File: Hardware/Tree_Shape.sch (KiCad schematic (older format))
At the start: 162 parts

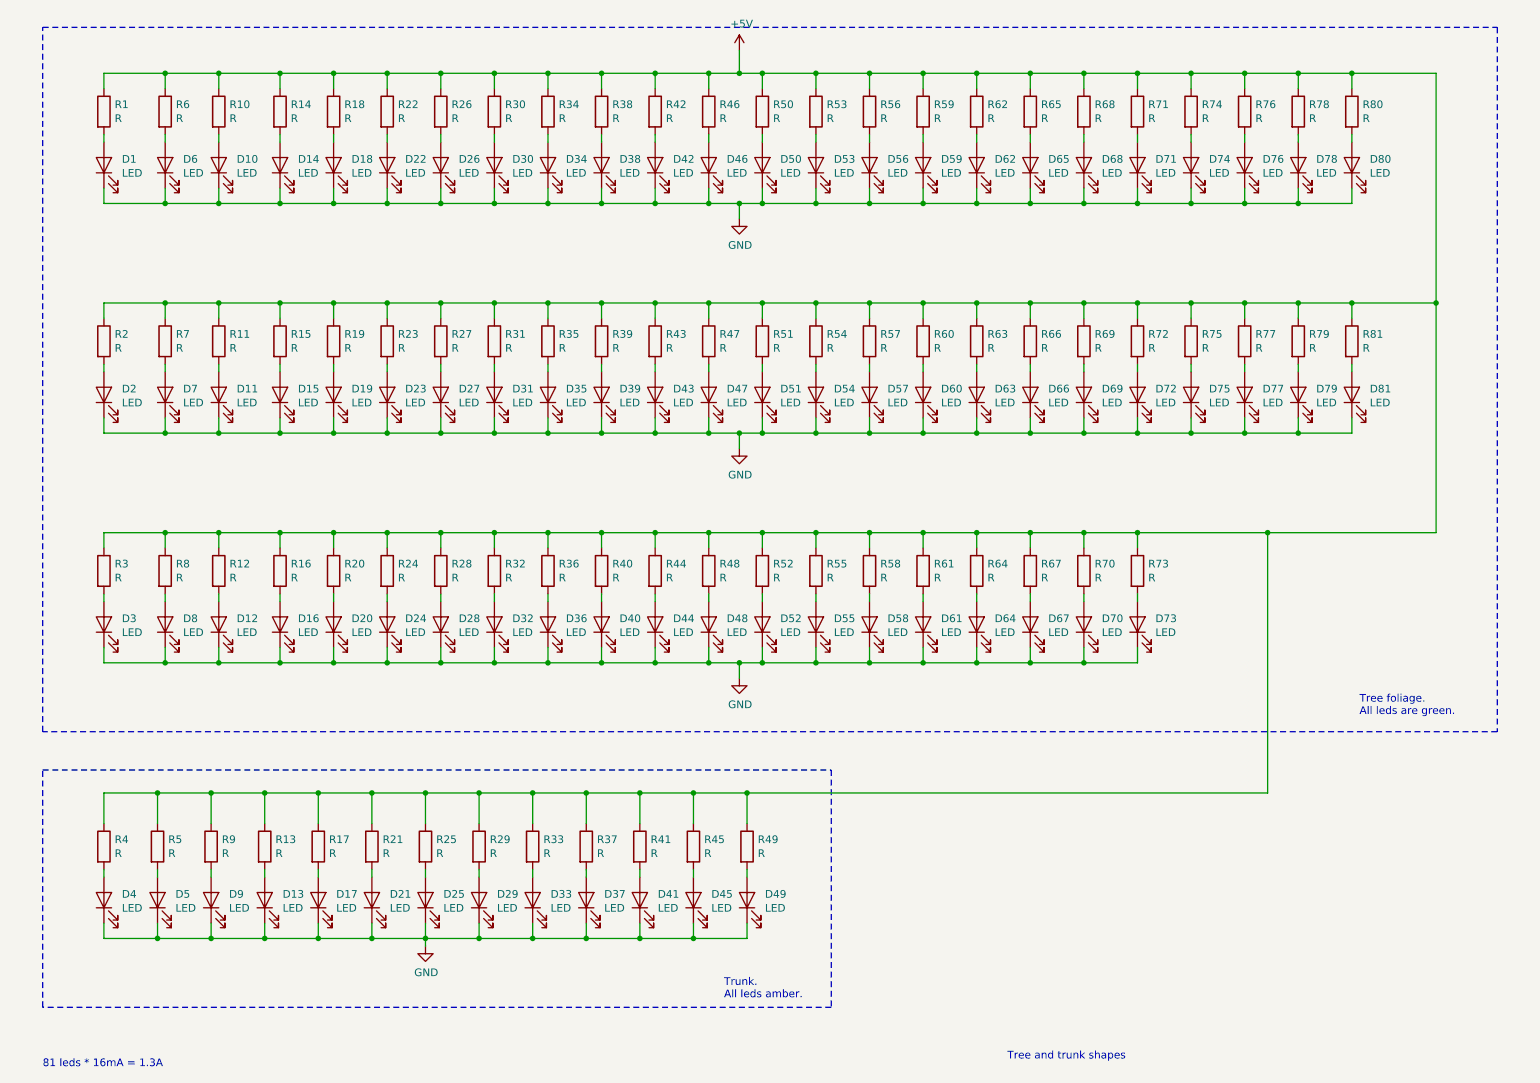
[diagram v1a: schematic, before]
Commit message: Set foliage and trunk leds color.
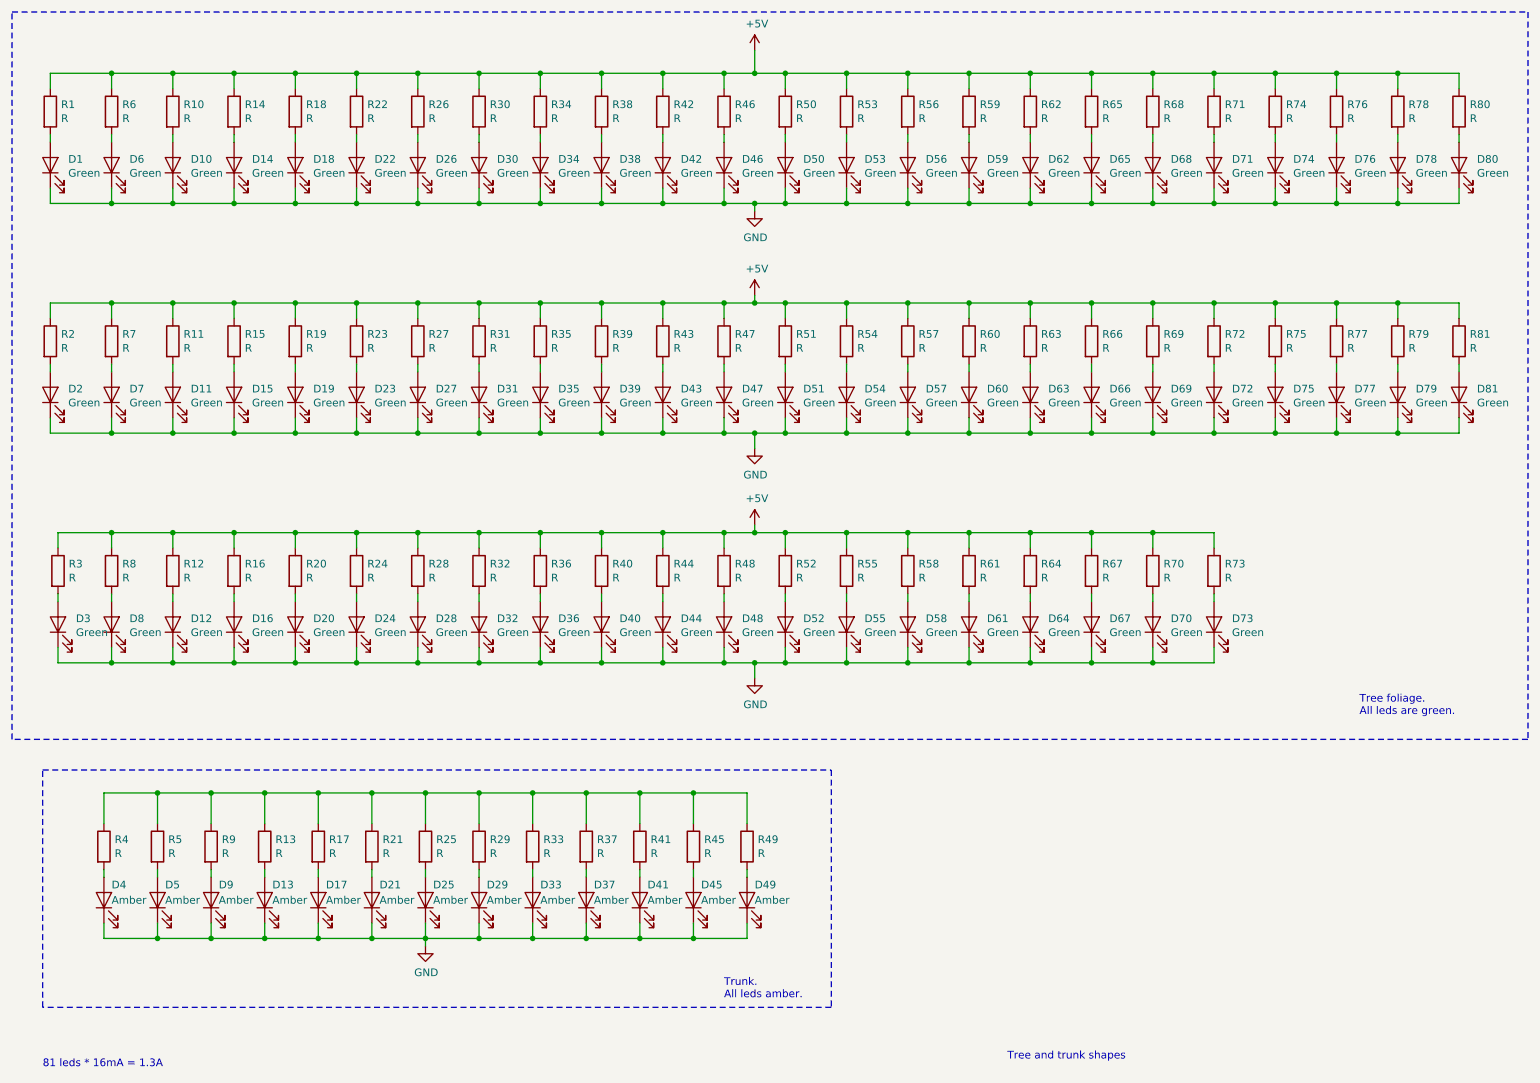
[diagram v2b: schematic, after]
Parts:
- D1, D10, D11, D12, D14, D15, D16, D18, D19, D2, D20, D22, D23, D24, D26, D27, D28, D3, D30, D31, D32, D34, D35, D36, D38, D39, D40, D42, D43, D44, D46, D47, D48, D50, D51, D52, D53, D54, D55, D56, D57, D58, D59, D6, D60, D61, D62, D63, D64, D65, D66, D67, D68, D69, D7, D70, D71, D72, D73, D74, D75, D76, D77, D78, D79, D8, D80, D81: value LED -> Green
- D13, D17, D21, D25, D29, D33, D37, D4, D41, D45, D49, D5, D9: value LED -> Amber
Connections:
- net +5V: no longer R13.1, R17.1, R21.1, R25.1, R29.1, R33.1, R37.1, R4.1, R41.1, R45.1, R49.1, R5.1, R9.1
- new net: R13.1, R17.1, R21.1, R25.1, R29.1, R33.1, R37.1, R4.1, R41.1, R45.1, R49.1, R5.1, R9.1
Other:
- moved on the sheet: D1, D10, D11, D12, D14, D15, D16, D18, D19, D2, D20, D22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

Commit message: Set foliage leds resistors value.
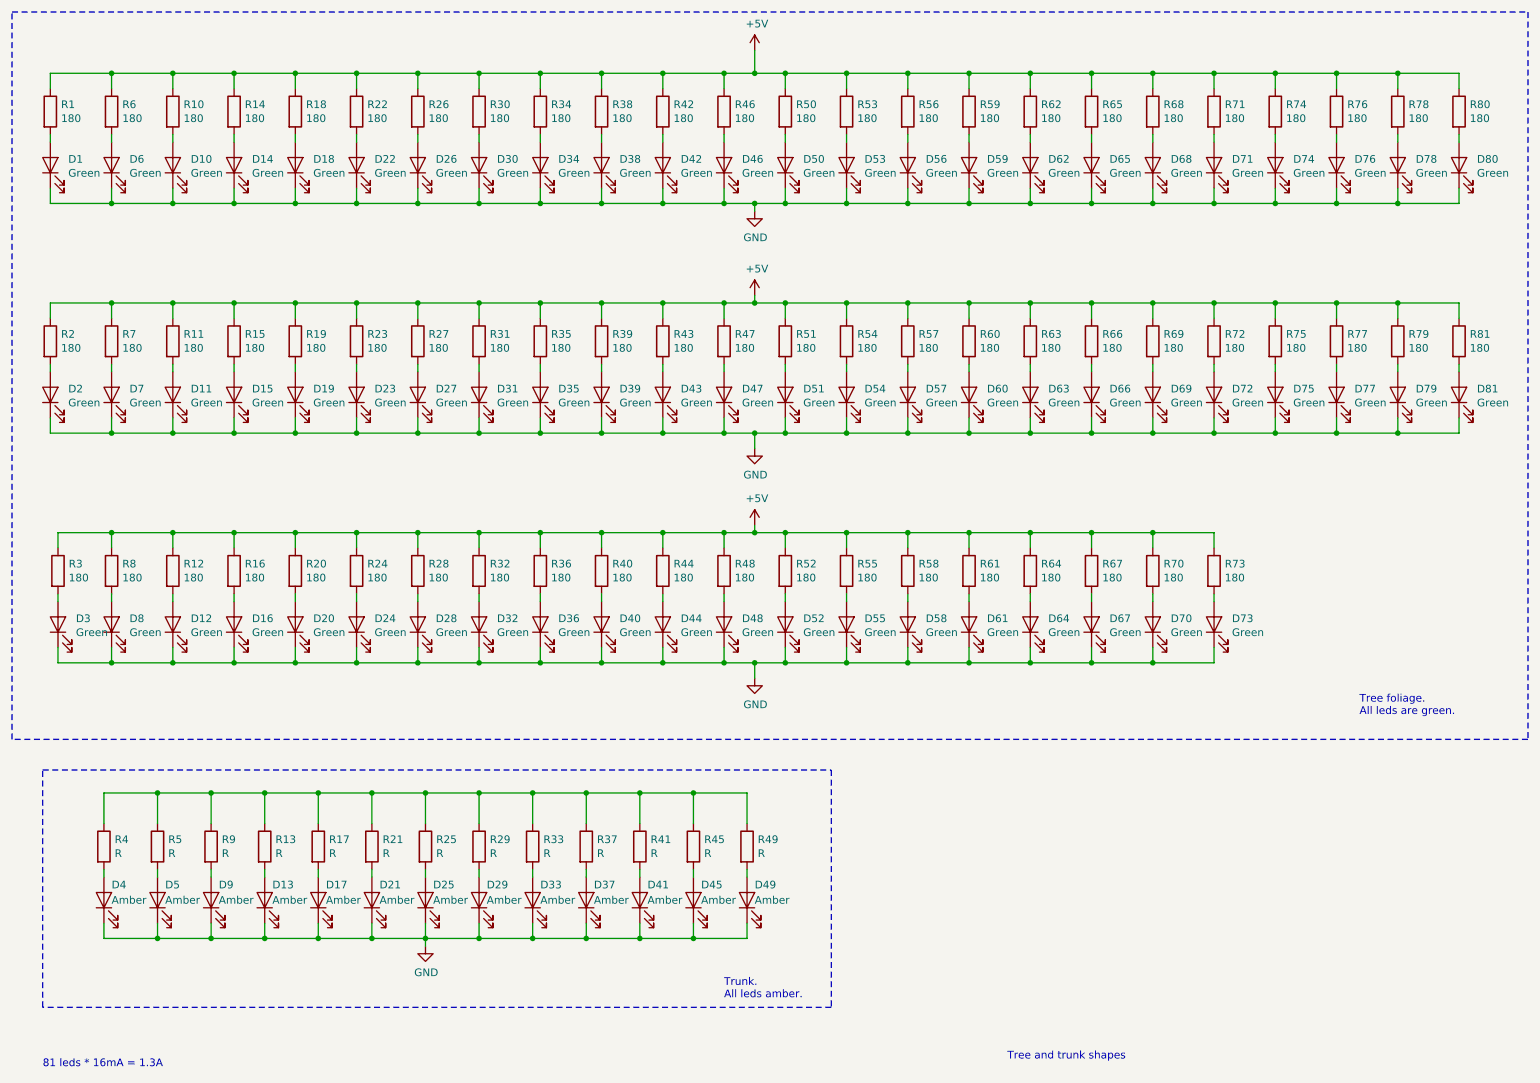
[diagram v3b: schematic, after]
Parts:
- R1, R10, R11, R12, R14, R15, R16, R18, R19, R2, R20, R22, R23, R24, R26, R27, R28, R3, R30, R31, R32, R34, R35, R36, R38, R39, R40, R42, R43, R44, R46, R47, R48, R50, R51, R52, R53, R54, R55, R56, R57, R58, R59, R6, R60, R61, R62, R63, R64, R65, R66, R67, R68, R69, R7, R70, R71, R72, R73, R74, R75, R76, R77, R78, R79, R8, R80, R81: value R -> 180

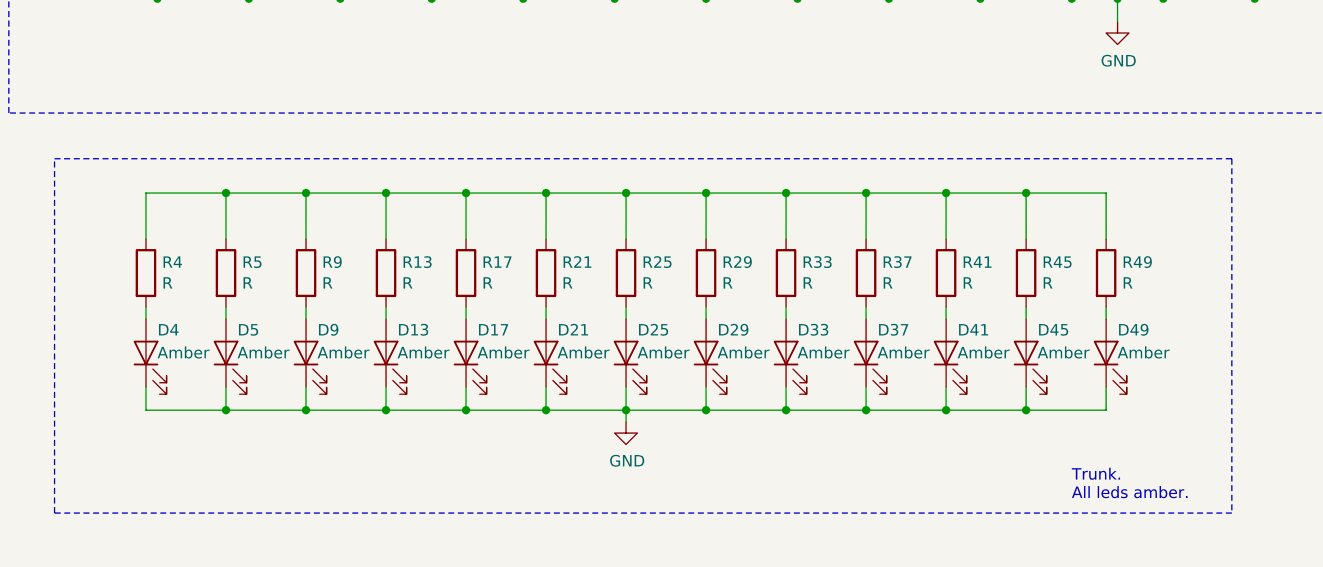
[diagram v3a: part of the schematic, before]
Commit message: Set trunk leds resistors value.
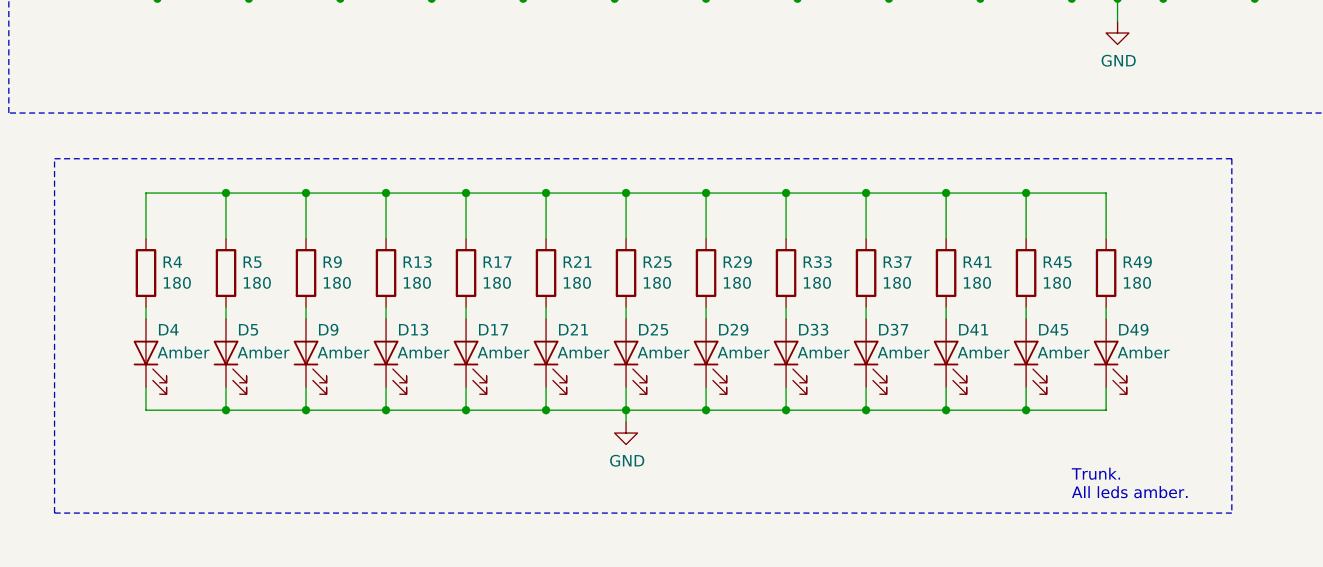
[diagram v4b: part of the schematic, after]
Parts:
- R13, R17, R21, R25, R29, R33, R37, R4, R41, R45, R49, R5, R9: value R -> 180
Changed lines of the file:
@@
 P 1450 6100
 F 0 "R4" H 1520 6146 50  0000 L CNN
-F 1 "R" H 1520 6055 50  0000 L CNN
+F 1 "180" H 1520 6055 50  0000 L CNN
 F 2 "Resistor_THT:R_Axial_DIN0207_L6.3mm_D2.5mm_P7.62mm_Horizontal" V 1380 6100 50  0001 C CNN
 F 3 "~" H 1450 6100 50  0001 C CNN
@@
 P 1800 6100
 F 0 "R5" H 1870 6146 50  0000 L CNN
-F 1 "R" H 1870 6055 50  0000 L CNN
+F 1 "180" H 1870 6055 50  0000 L CNN
 F 2 "Resistor_THT:R_Axial_DIN0207_L6.3mm_D2.5mm_P7.62mm_Horizontal" V 1730 6100 50  0001 C CNN
 F 3 "~" H 1800 6100 50  0001 C CNN
@@
 P 2150 6100
 F 0 "R9" H 2220 6146 50  0000 L CNN
-F 1 "R" H 2220 6055 50  0000 L CNN
+F 1 "180" H 2220 6055 50  0000 L CNN
 F 2 "Resistor_THT:R_Axial_DIN0207_L6.3mm_D2.5mm_P7.62mm_Horizontal" V 2080 6100 50  0001 C CNN
 F 3 "~" H 2150 6100 50  0001 C CNN
@@
 P 2500 6100
 F 0 "R13" H 2570 6146 50  0000 L CNN
-F 1 "R" H 2570 6055 50  0000 L CNN
+F 1 "180" H 2570 6055 50  0000 L CNN
 F 2 "Resistor_THT:R_Axial_DIN0207_L6.3mm_D2.5mm_P7.62mm_Horizontal" V 2430 6100 50  0001 C CNN
 F 3 "~" H 2500 6100 50  0001 C CNN
@@
 P 2850 6100
 F 0 "R17" H 2920 6146 50  0000 L CNN
-F 1 "R" H 2920 6055 50  0000 L CNN
+F 1 "180" H 2920 6055 50  0000 L CNN
 F 2 "Resistor_THT:R_Axial_DIN0207_L6.3mm_D2.5mm_P7.62mm_Horizontal" V 2780 6100 50  0001 C CNN
 F 3 "~" H 2850 6100 50  0001 C CNN
@@
 P 3200 6100
 F 0 "R21" H 3270 6146 50  0000 L CNN
-F 1 "R" H 3270 6055 50  0000 L CNN
+F 1 "180" H 3270 6055 50  0000 L CNN
 F 2 "Resistor_THT:R_Axial_DIN0207_L6.3mm_D2.5mm_P7.62mm_Horizontal" V 3130 6100 50  0001 C CNN
 F 3 "~" H 3200 6100 50  0001 C CNN
@@
 P 3550 6100
 F 0 "R25" H 3620 6146 50  0000 L CNN
-F 1 "R" H 3620 6055 50  0000 L CNN
+F 1 "180" H 3620 6055 50  0000 L CNN
 F 2 "Resistor_THT:R_Axial_DIN0207_L6.3mm_D2.5mm_P7.62mm_Horizontal" V 3480 6100 50  0001 C CNN
 F 3 "~" H 3550 6100 50  0001 C CNN
@@
 P 3900 6100
 F 0 "R29" H 3970 6146 50  0000 L CNN
-F 1 "R" H 3970 6055 50  0000 L CNN
+F 1 "180" H 3970 6055 50  0000 L CNN
 F 2 "Resistor_THT:R_Axial_DIN0207_L6.3mm_D2.5mm_P7.62mm_Horizontal" V 3830 6100 50  0001 C CNN
 F 3 "~" H 3900 6100 50  0001 C CNN
@@
 P 4250 6100
 F 0 "R33" H 4320 6146 50  0000 L CNN
-F 1 "R" H 4320 6055 50  0000 L CNN
+F 1 "180" H 4320 6055 50  0000 L CNN
 F 2 "Resistor_THT:R_Axial_DIN0207_L6.3mm_D2.5mm_P7.62mm_Horizontal" V 4180 6100 50  0001 C CNN
 F 3 "~" H 4250 6100 50  0001 C CNN
@@
 P 4600 6100
 F 0 "R37" H 4670 6146 50  0000 L CNN
-F 1 "R" H 4670 6055 50  0000 L CNN
+F 1 "180" H 4670 6055 50  0000 L CNN
 F 2 "Resistor_THT:R_Axial_DIN0207_L6.3mm_D2.5mm_P7.62mm_Horizontal" V 4530 6100 50  0001 C CNN
 F 3 "~" H 4600 6100 50  0001 C CNN
@@
 P 4950 6100
 F 0 "R41" H 5020 6146 50  0000 L CNN
-F 1 "R" H 5020 6055 50  0000 L CNN
+F 1 "180" H 5020 6055 50  0000 L CNN
 F 2 "Resistor_THT:R_Axial_DIN0207_L6.3mm_D2.5mm_P7.62mm_Horizontal" V 4880 6100 50  0001 C CNN
 F 3 "~" H 4950 6100 50  0001 C CNN
@@
 P 5300 6100
 F 0 "R45" H 5370 6146 50  0000 L CNN
-F 1 "R" H 5370 6055 50  0000 L CNN
+F 1 "180" H 5370 6055 50  0000 L CNN
 F 2 "Resistor_THT:R_Axial_DIN0207_L6.3mm_D2.5mm_P7.62mm_Horizontal" V 5230 6100 50  0001 C CNN
 F 3 "~" H 5300 6100 50  0001 C CNN
@@
 P 5650 6100
 F 0 "R49" H 5720 6146 50  0000 L CNN
-F 1 "R" H 5720 6055 50  0000 L CNN
+F 1 "180" H 5720 6055 50  0000 L CNN
 F 2 "Resistor_THT:R_Axial_DIN0207_L6.3mm_D2.5mm_P7.62mm_Horizontal" V 5580 6100 50  0001 C CNN
 F 3 "~" H 5650 6100 50  0001 C CNN
